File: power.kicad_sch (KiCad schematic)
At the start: 30 parts, among them U3 TPS54560BDDA, U4 AP7361C-33E, U5 AP7361C-33E, U7 DSF105Q9R0HDR

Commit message: Power Supply Speccing, IMU, Eyeballs
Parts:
- C15, C16, C20, C21: value C -> 47u
- C17: value C -> 0.1u
- L1: value L -> 22u
- R10: value R_US -> 18k
- R12: value R_US -> 82k
- R9: value R_US -> 62k
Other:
- note added: "Add Primary UVLO IC to prevent discharge below 6V2!"
- note added: "Select C17 voltage rating >10V per datasheet"
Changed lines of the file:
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@@
 		)
 	)
+	(text "Add Primary UVLO IC to prevent discharge below 6V2!"
+		(exclude_from_sim no)
+		(at 48.768 71.12 0)
+		(effects
+			(font
+				(size 1.27 1.27)
+				(color 255 0 0 1)
+			)
+		)
+	)
 	(text "Header (likely DNP) for battery charging."
 		(exclude_from_sim no)
@@
 		)
 	)
+	(text "Select C17 voltage rating >10V per datasheet"
+		(exclude_from_sim no)
+		(at 242.316 77.724 0)
+		(effects
+			(font
+				(size 1.27 1.27)
+				(color 255 127 0 1)
+			)
+		)
+	)
 	(text "Replace with toggle version?"
 		(exclude_from_sim no)
@@
 			)
 		)
-		(property "Value" "C"
+		(property "Value" "47u"
 			(at 278.13 109.22 0)
 			(effects
@@
 			)
 		)
-		(property "Datasheet" "~"
+		(property "Datasheet" "https://calchip.com/wp-content/uploads/2023/09/GMC-Series-2.pdf"
 			(at 275.59 107.95 0)
 			(effects
@@
 			)
 		)
-		(property "Description" "Unpolarized capacitor"
+		(property "Description" "GMC21X5R476M10NT"
 			(at 275.59 107.95 0)
 			(effects
@@
 			)
 		)
-		(property "Value" "R_US"
+		(property "Value" "62k"
 			(at 312.42 110.4899 0)
 			(effects
@@
 			)
 		)
-		(property "Value" "C"
+		(property "Value" "47u"
 			(at 295.91 109.22 0)
 			(effects
@@
 			)
 		)
-		(property "Datasheet" "~"
+		(property "Datasheet" "https://calchip.com/wp-content/uploads/2023/09/GMC-Series-2.pdf"
 			(at 293.37 107.95 0)
 			(effects
@@
 			)
 		)
-		(property "Description" "Unpolarized capacitor"
+		(property "Description" "GMC21X5R476M10NT"
 			(at 293.37 107.95 0)
 			(effects
@@
 			)
 		)
-		(property "Value" "R_US"
+		(property "Value" "82k"
 			(at 209.55 116.8399 0)
 			(effects
@@
 			)
 		)
-		(property "Value" "R_US"
+		(property "Value" "18k"
 			(at 312.42 123.1899 0)
 			(effects
@@
 			)
 		)
-		(property "Value" "C"
+		(property "Value" "47u"
 			(at 269.24 109.22 0)
 			(effects
@@
 			)
 		)
-		(property "Datasheet" "~"
+		(property "Datasheet" "https://calchip.com/wp-content/uploads/2023/09/GMC-Series-2.pdf"
 			(at 266.7 107.95 0)
 			(effects
@@
 			)
 		)
-		(property "Description" "Unpolarized capacitor"
+		(property "Description" "GMC21X5R476M10NT"
 			(at 266.7 107.95 0)
 			(effects
@@
 			)
 		)
-		(property "Value" "C"
+		(property "Value" "47u"
 			(at 287.02 109.22 0)
 			(effects
@@
 			)
 		)
-		(property "Datasheet" "~"
+		(property "Datasheet" "https://calchip.com/wp-content/uploads/2023/09/GMC-Series-2.pdf"
 			(at 284.48 107.95 0)
 			(effects
@@
 			)
 		)
-		(property "Description" "Unpolarized capacitor"
+		(property "Description" "GMC21X5R476M10NT"
 			(at 284.48 107.95 0)
 			(effects
@@
 			)
 		)
-		(property "Value" "L"
+		(property "Value" "22u"
 			(at 254 101.6 90)
 			(effects
@@
 			)
 		)
-		(property "Datasheet" "~"
+		(property "Datasheet" "https://www.we-online.com/components/products/datasheet/78404084220.pdf"
 			(at 254 104.14 0)
 			(effects
@@
 			)
 		)
-		(property "Value" "C"
+		(property "Value" "0.1u"
 			(at 238.76 93.98 90)
 			(effects

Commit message: Release Candidate 1
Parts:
- added J5: Conn_01x03_Socket, Connector_JST:JST_XH_B3B-XH-A_1x03_P2.50mm_Vertical, symbol Connector:Conn_01x03_Socket
- added Q1: DMG2302U, Package_TO_SOT_SMD:SOT-23, symbol Transistor_FET:DMG2302U
- added Q2, Q4, Q5: Si2319CDS, Package_TO_SOT_SMD:SOT-23, symbol Transistor_FET:Si2319CDS
- added R28: 10k, symbol Device:R_US
- added R32: 56k, Resistor_SMD:R_0805_2012Metric, symbol Device:R_US
- added R33, R34: 100k, Resistor_SMD:R_0805_2012Metric, symbol Device:R_US
- added SW9: SW_SPDT_321, 0_airbrake_footprints:CL-SB-12A-01T, symbol Switch:SW_SPDT_321
- added U10: BD4860G-TR, Package_TO_SOT_SMD:SOT-23-5, symbol Power_Management:BD48ExxG
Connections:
- net +BATT: now also J5.1 (Pin_1), Q4.2 (S), Q5.2 (S), R32.1, U10.2 (VDD); no longer D4.2 (A)
- net -BATT: now also J5.3 (Pin_3), Q1.2 (S), R34.2, U10.3 (GND)
- net BATT_TAP: now also J5.2 (Pin_2)
- new net: Q4.1 (G), Q5.1 (G), R32.2, SW9.3 (A)
- new net: Q1.3 (D), Q2.1 (G), R28.1
- new net +BATT_SW: D4.2 (A), Q2.2 (S), Q4.3 (D), Q5.3 (D), R28.2
- new net BAT_OK: R33.1, SW9.2 (B), U10.1 (VOUT)
- new net BAT_OK_MCU: R33.2, R34.1
- new net SERVO+: Q2.3 (D)
- new net SERVO_EN: Q1.1 (G)
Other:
- note added: "Charge Plug"
- note added: "LVCO/Power Switch"
- note added: "Servo Power Enable"
- note added: "https://www.digikey.com/en/products/detail/rohm-semiconductor/BD4860G-TR/2749952"
- note removed: "Add Primary UVLO IC to prevent discharge below 6V2!"
- note removed: "Header (likely DNP) for battery charging."
- note removed: "Power Switch"
- note removed: "Replace with toggle version?"
- moved on the sheet: C10, C11, C12, C13, C14, C15, C16, C17, C18, C19, C20, C21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

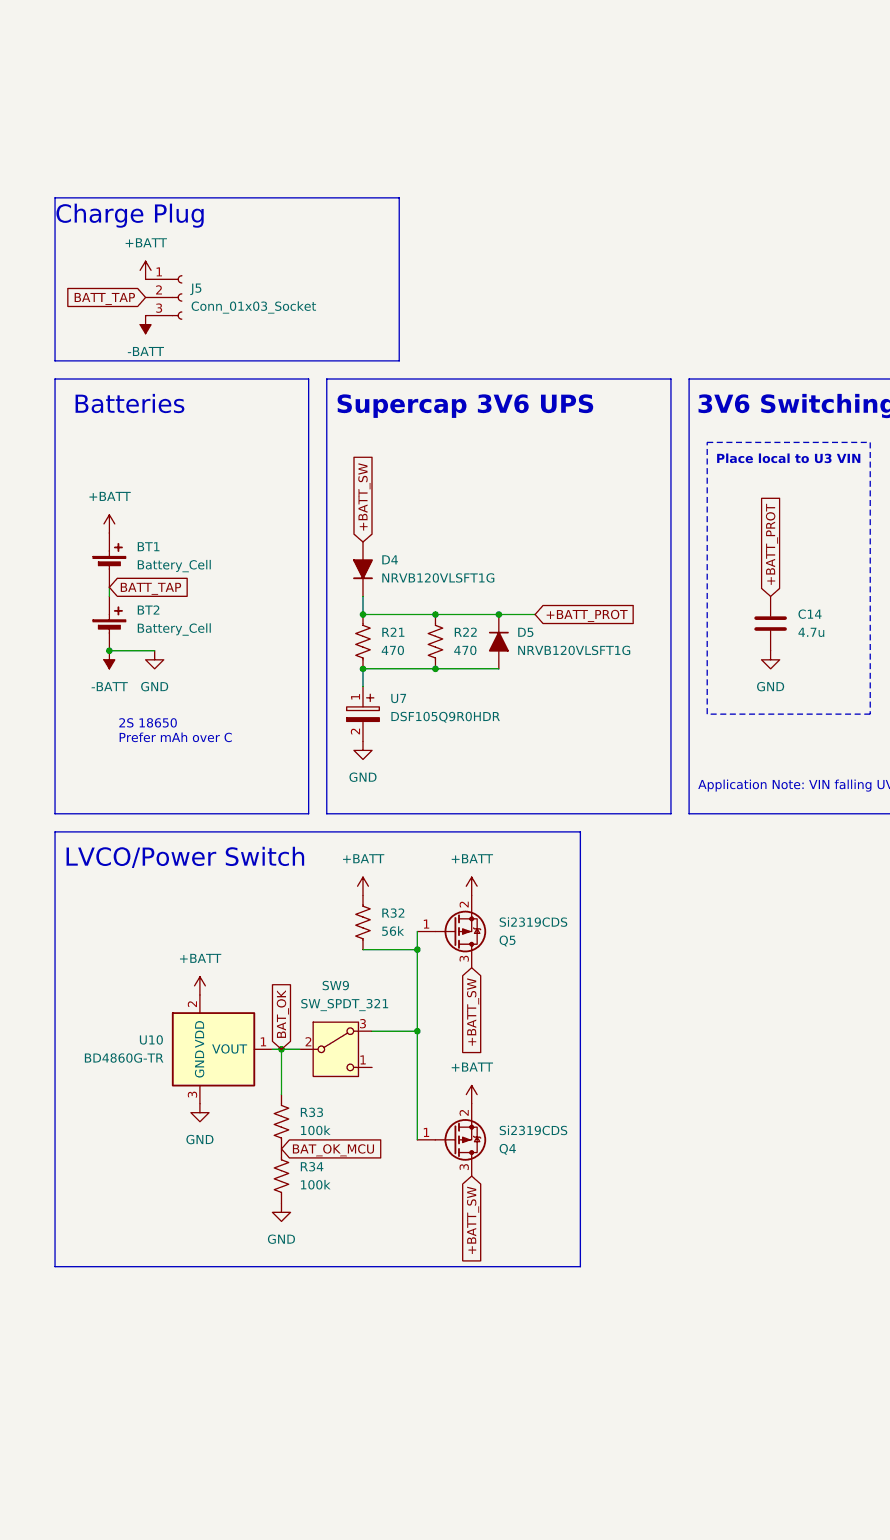
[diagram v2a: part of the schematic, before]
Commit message: Release Candidate 2
Incorporates fixes for all identified issues in the PCBR
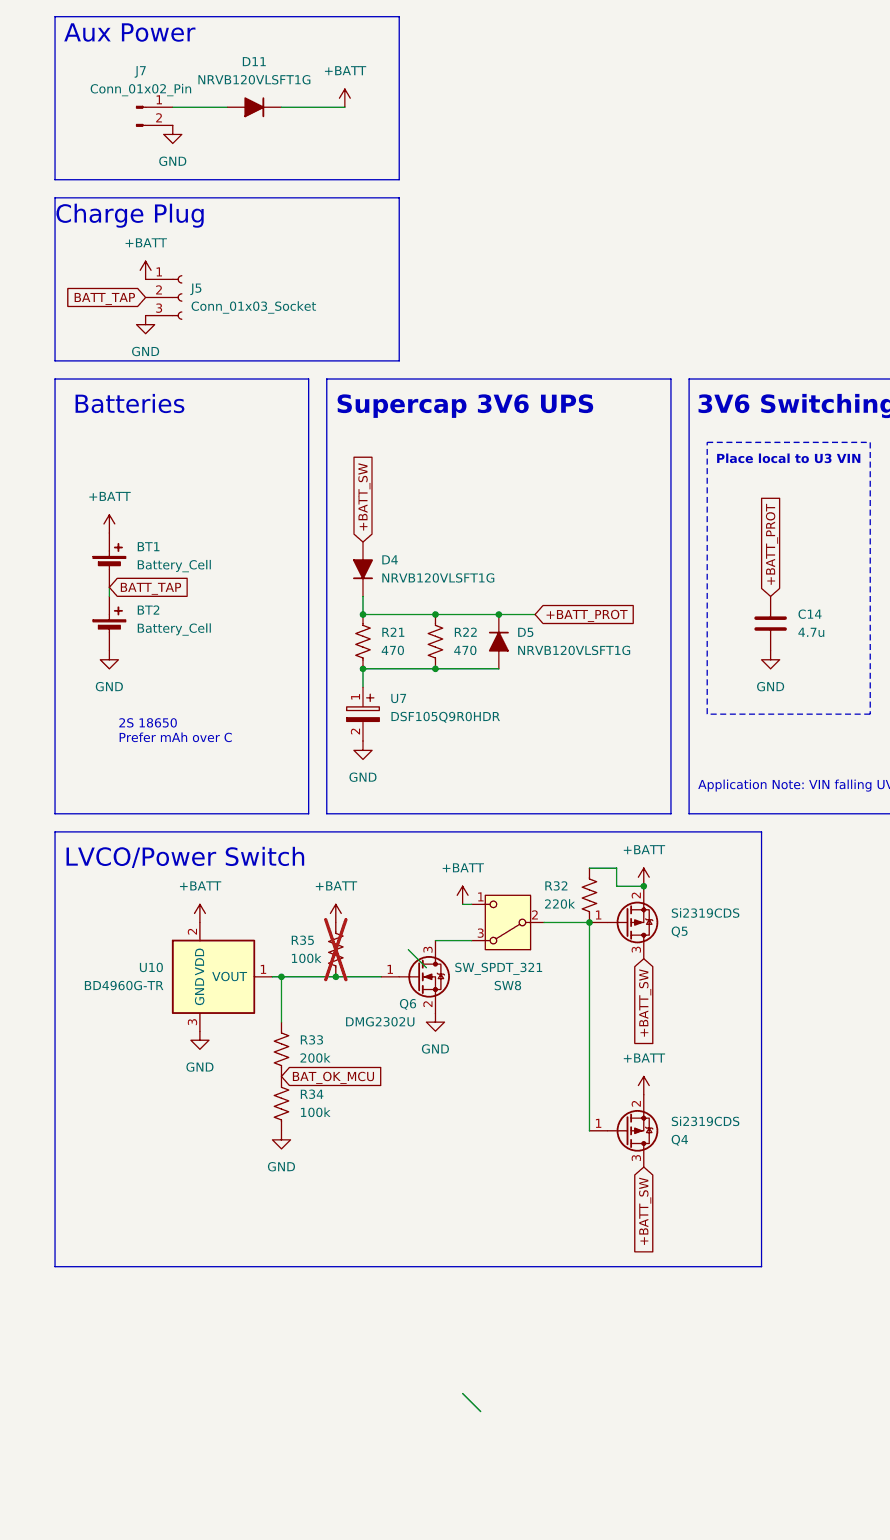
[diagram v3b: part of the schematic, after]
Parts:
- removed SW9: SW_SPDT_321, 0_airbrake_footprints:CL-SB-12A-01T, symbol Switch:SW_SPDT_321
- added D11: NRVB120VLSFT1G, Diode_SMD:D_SOD-123F, symbol Device:D_Filled
- added J7: Conn_01x02_Pin, Connector_PinHeader_2.54mm:PinHeader_1x02_P2.54mm_Vertical, symbol Connector:Conn_01x02_Pin
- added Q6: DMG2302U, Package_TO_SOT_SMD:SOT-23, symbol Transistor_FET:DMG2302U
- added R35: 100k, Resistor_SMD:R_0805_2012Metric, symbol Device:R_US
- added SW8: SW_SPDT_321, 0_airbrake_footprints:CL-SB-12A-01T, symbol Switch:SW_SPDT_321
- R28: footprint (none) -> Resistor_SMD:R_0805_2012Metric
- R32: value 56k -> 220k
- R33: value 100k -> 200k
- U10: value BD4860G-TR -> BD4960G-TR
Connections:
- net +BATT: now also D11.1 (K), R35.1, SW8.1 (C)
- net at Q4.1 (G), Q5.1 (G), R32.2: now also SW8.2 (B)
- net -BATT renamed GND
- net GND: now also J7.2 (Pin_2), Q6.2 (S)
- net BAT_OK: no longer names the net of R33.1, U10.1 (VOUT)
- net BAT_OK: now also Q6.1 (G), R35.2
- new net: Q6.3 (D), SW8.3 (A)
- new net: D11.2 (A), J7.1 (Pin_1)
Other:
- note added: "Aux Power"
- moved on the sheet: Q4, Q5, R33, R34, U10

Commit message: Release Candidate 3
Fixed name, one location with vias. Added production files in prep for merge request.
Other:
- title: Airbrakes PCB - Earendel -> Airbrakes PCB - Veðrfölnir 
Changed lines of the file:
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@@
 	(paper "B")
 	(title_block
-		(title "Airbrakes PCB - Earendel")
+		(title "Airbrakes PCB - Veðrfölnir ")
 		(date "2025-02-18")
 		(rev "v2025.01A")
